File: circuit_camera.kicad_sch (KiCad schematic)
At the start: 25 parts, among them U10 LDO_5-1.8V-(MIC5504-1.8YM5-TR), U8 LM2576HVS-5, U9 LDO 5-3.3V-(MIC5504-3.3YM5-TR)

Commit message: Début PCB
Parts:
- added S1: Switch-SPDT-(EG1218), GAUL-Empreintes:switch-(SW_EG1218), symbol GAUL-Symboles:Switch-SPDT-(EG1218)
- C1LDO1, C1LDO2, C2LDO1, C2LDO2: footprint GAUL-Empreintes:cap-1uF-(CAPC0603X35N) -> Capacitor_SMD:C_0603_1608Metric_Pad1.08x0.95mm_HandSolder
- D1, D4: footprint (none) -> Diode_SMD:D_0603_1608Metric_Pad1.05x0.95mm_HandSolder
- F1, F2: value PTC_resettable_fuse_(MF-MSMF030-2) -> xxmA; footprint MF-MSMF030-2:FUSER_MF-MSMF030-2 -> Fuse:Fuse_0603_1608Metric_Pad1.05x0.95mm_HandSolder
- FB1: footprint (none) -> Inductor_SMD:L_0603_1608Metric_Pad1.05x0.95mm_HandSolder
- Lout1: footprint LM2576:IND_YUDEN_NS12575_YDN -> GAUL-Empreintes:induct-100uH-(IND_YUDEN_NS12575_YDN)
- R30, R31, R32: footprint GAUL-Empreintes:Resistance_TH_classique -> Resistor_SMD:R_0603_1608Metric
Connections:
- net +3.3V: now also S1.2; no longer C2LDO1.1, Cout1.1, Lout1.2, U8.4 (FB), U9.5 (VOUT)
- net GND: now also bornier1.1; no longer bornier1.0 (GND)
- net at F1.1: now also bornier1.2; no longer bornier1.1 (Vbatterie)
- new net: Cout1.1, Lout1.2, S1.1, U8.4 (FB)
- new net: C2LDO1.1, S1.3, U9.5 (VOUT)

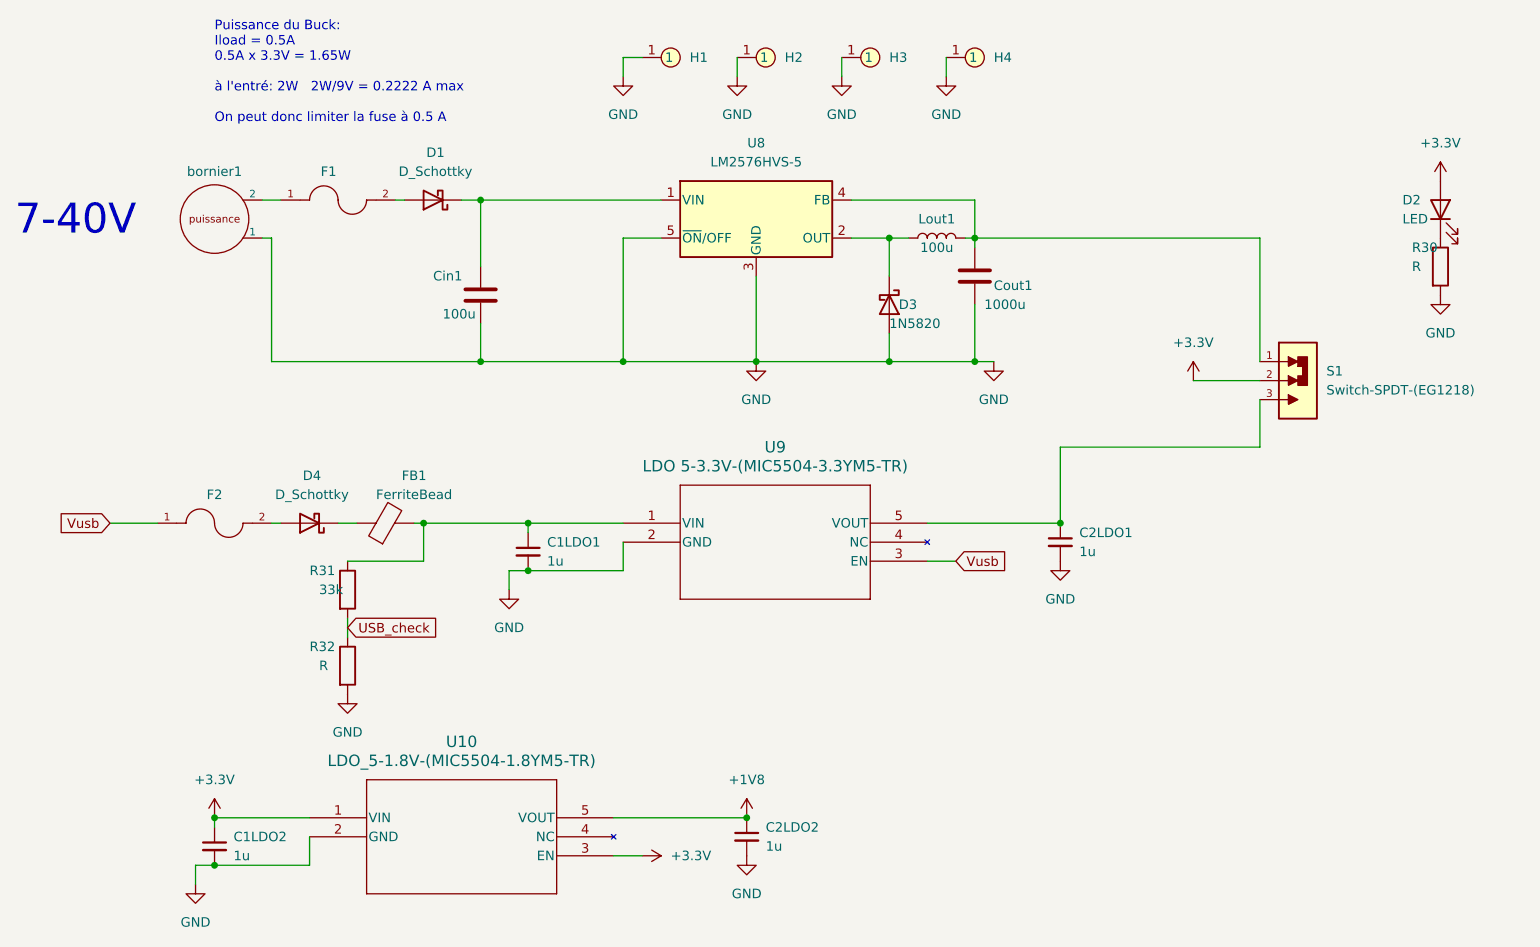
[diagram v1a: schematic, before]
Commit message: Remplacement du Buck par un LDO
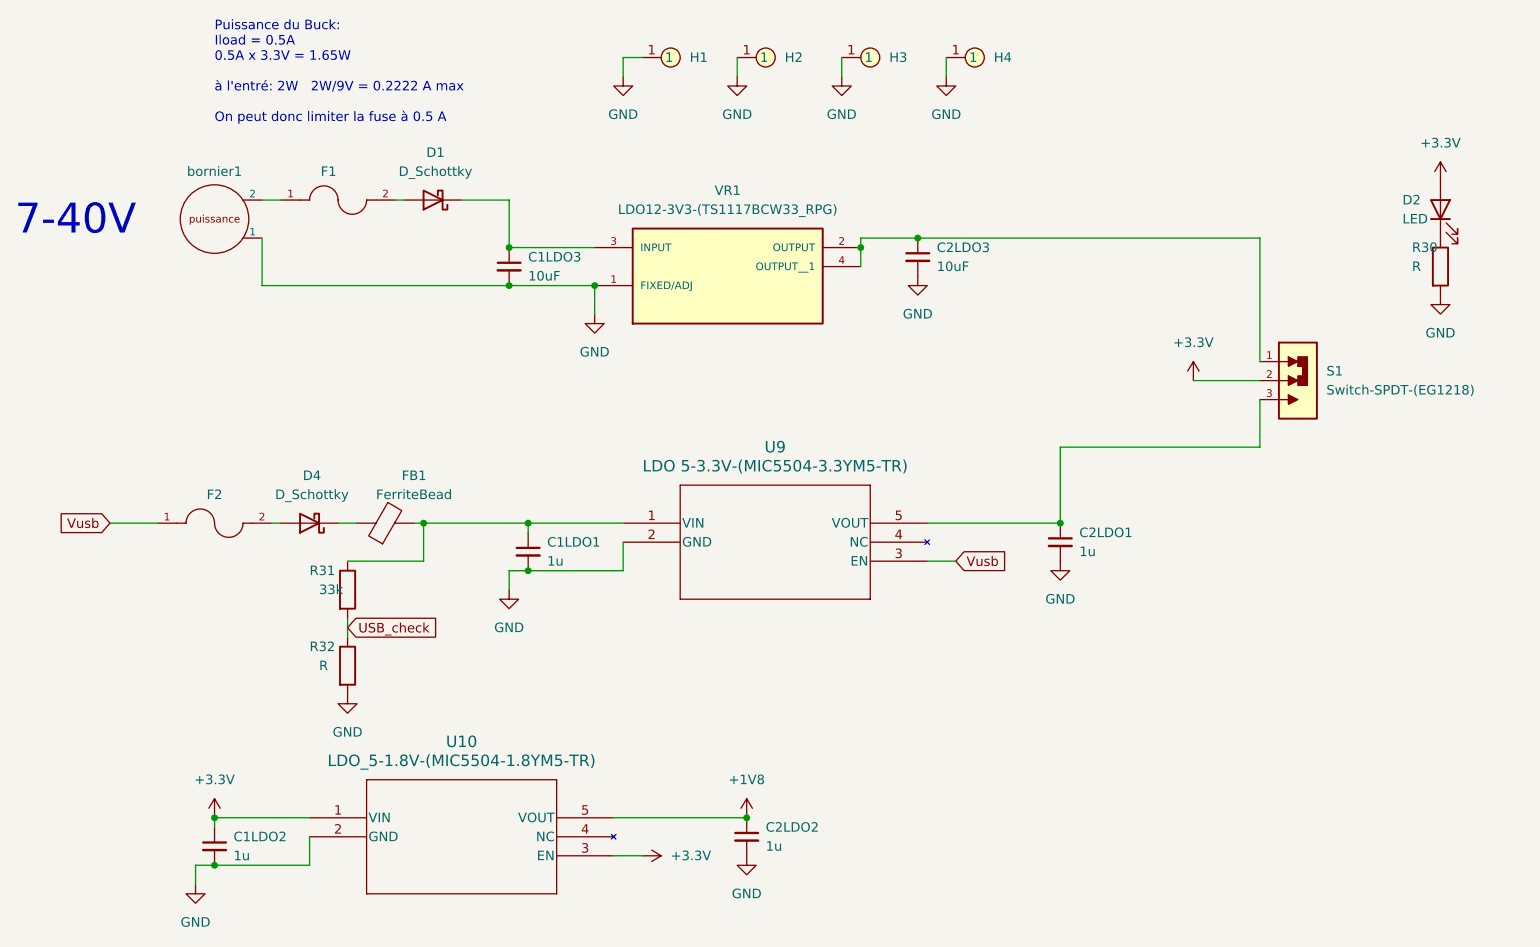
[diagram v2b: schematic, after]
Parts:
- removed Cin1: 100u, Capacitor_THT:CP_Radial_D8.0mm_P3.50mm, symbol Device:C
- removed Cout1: 1000u, Capacitor_THT:CP_Radial_D10.0mm_P5.00mm, symbol Device:C
- removed D3: 1N5820, Diode_THT:D_DO-201AD_P15.24mm_Horizontal, symbol Diode:1N5820
- removed Lout1: 100u, GAUL-Empreintes:induct-100uH-(IND_YUDEN_NS12575_YDN), symbol Device:L
- removed U8: LM2576HVS-5, Package_TO_SOT_SMD:TO-263-5_TabPin3, symbol Regulator_Switching:LM2576HVS-5
- added C1LDO3, C2LDO3: 10uF, Capacitor_SMD:C_0603_1608Metric_Pad1.08x0.95mm_HandSolder, symbol Device:C_Small
- added VR1: LDO12-3V3-(TS1117BCW33_RPG), GAUL-Empreintes:LDO12-3V3-(TS1117BCW33_RPG), symbol GAUL-Symboles:LDO12-3V3-(TS1117BCW33_RPG)
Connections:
- net GND: now also C1LDO3.2, C2LDO3.2, VR1.1 (FIXED/ADJ)
- net at S1.1: now also C2LDO3.1, VR1.2 (OUTPUT), VR1.4 (OUTPUT__1)
- net at D1.1 (K): now also C1LDO3.1, VR1.3 (INPUT)

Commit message: Routing terminé
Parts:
- added H5, H6, H7, H8: ~, GAUL-Empreintes:Ground_mounting_hole_1mm, symbol GAUL-Symboles:Ground_mounting_hole_1mm
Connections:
- net GND: now also H5.1, H6.1, H7.1, H8.1
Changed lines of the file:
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@@
+    (stroke (width 0) (type default))
+  )
+  (wire (pts (xy 196.85 69.85) (xy 196.85 67.31))
     (stroke (width 0) (type default))
   )
@@
     (stroke (width 0) (type default))
   )
+  (wire (pts (xy 227.33 69.85) (xy 227.33 67.31))
+    (stroke (width 0) (type default))
+  )
   (wire (pts (xy 111.76 97.79) (xy 123.19 97.79))
     (stroke (width 0) (type default))
@@
     (stroke (width 0) (type default))
   )
+  (wire (pts (xy 212.09 69.85) (xy 212.09 67.31))
+    (stroke (width 0) (type default))
+  )
   (wire (pts (xy 69.85 175.26) (xy 72.39 175.26))
     (stroke (width 0) (type default))
@@
   )
   (wire (pts (xy 114.3 129.54) (xy 127 129.54))
+    (stroke (width 0) (type default))
+  )
+  (wire (pts (xy 182.88 69.85) (xy 182.88 67.31))
     (stroke (width 0) (type default))
   )
@@
     )
   )
+  (symbol (lib_id "GAUL-Symboles:Ground_mounting_hole_1mm") (at 215.9 64.77 180) (unit 1)
+    (in_bom yes) (on_board yes) (dnp no) (fields_autoplaced)
+    (property "Reference" "H7" (at 218.44 67.31 0)
+      (effects (font (size 1.27 1.27)) (justify right))
+    )
+    (property "Value" "~" (at 215.9 64.77 0)
+      (effects (font (size 1.27 1.27)))
+    )
+    (property "Footprint" "GAUL-Empreintes:Ground_mounting_hole_1mm" (at 215.9 64.77 0)
+      (effects (font (size 1.27 1.27)) hide)
+    )
+    (property "Datasheet" "" (at 215.9 64.77 0)
+      (effects (font (size 1.27 1.27)) hide)
+    )
+    (pin "1")
+    (instances
+      (project "Payload"
+        (path "/5f62c44b-34ee-4720-b187-b4a520863a8a/b731aecd-8fa5-4432-90a5-bb6d0ae39f62"
+          (reference "H7") (unit 1)
+        )
+      )
+      (project "Buck_5V"
+        (path "/b57e233b-724e-41fe-b467-3bde33ee5ca1"
+          (reference "H?") (unit 1)
+        )
+      )
+    )
+  )
   (symbol (lib_id "GAUL-Symboles:Ground_mounting_hole_1mm") (at 133.35 64.77 180) (unit 1)
     (in_bom yes) (on_board yes) (dnp no) (fields_autoplaced)
@@
     )
   )
+  (symbol (lib_id "GAUL-Symboles:Ground_mounting_hole_1mm") (at 186.69 64.77 180) (unit 1)
+    (in_bom yes) (on_board yes) (dnp no) (fields_autoplaced)
+    (property "Reference" "H5" (at 189.23 67.31 0)
+      (effects (font (size 1.27 1.27)) (justify right))
+    )
+    (property "Value" "~" (at 186.69 64.77 0)
+      (effects (font (size 1.27 1.27)))
+    )
+    (property "Footprint" "GAUL-Empreintes:Ground_mounting_hole_1mm" (at 186.69 64.77 0)
+      (effects (font (size 1.27 1.27)) hide)
+    )
+    (property "Datasheet" "" (at 186.69 64.77 0)
+      (effects (font (size 1.27 1.27)) hide)
+    )
+    (pin "1")
+    (instances
+      (project "Payload"
+        (path "/5f62c44b-34ee-4720-b187-b4a520863a8a/b731aecd-8fa5-4432-90a5-bb6d0ae39f62"
+          (reference "H5") (unit 1)
+        )
+      )
+      (project "Buck_5V"
+        (path "/b57e233b-724e-41fe-b467-3bde33ee5ca1"
+          (reference "H?") (unit 1)
+        )
+      )
+    )
+  )
   (symbol (lib_id "power:GND") (at 156.21 69.85 0) (unit 1)
     (in_bom yes) (on_board yes) (dnp no) (fields_autoplaced)
@@
     )
   )
+  (symbol (lib_id "power:GND") (at 196.85 69.85 0) (unit 1)
+    (in_bom yes) (on_board yes) (dnp no) (fields_autoplaced)
+    (property "Reference" "#PWR0145" (at 196.85 76.2 0)
+      (effects (font (size 1.27 1.27)) hide)
+    )
+    (property "Value" "GND" (at 196.85 74.93 0)
+      (effects (font (size 1.27 1.27)))
+    )
+    (property "Footprint" "" (at 196.85 69.85 0)
+      (effects (font (size 1.27 1.27)) hide)
+    )
+    (property "Datasheet" "" (at 196.85 69.85 0)
+      (effects (font (size 1.27 1.27)) hide)
+    )
+    (pin "1")
+    (instances
+      (project "Payload"
+        (path "/5f62c44b-34ee-4720-b187-b4a520863a8a/b731aecd-8fa5-4432-90a5-bb6d0ae39f62"
+          (reference "#PWR0145") (unit 1)
+        )
+      )
+      (project "Buck_5V"
+        (path "/b57e233b-724e-41fe-b467-3bde33ee5ca1"
+          (reference "#PWR?") (unit 1)
+        )
+      )
+    )
+  )
   (symbol (lib_id "GAUL-Symboles:Ground_mounting_hole_1mm") (at 160.02 64.77 180) (unit 1)
     (in_bom yes) (on_board yes) (dnp no) (fields_autoplaced)
@@
     )
   )
+  (symbol (lib_id "GAUL-Symboles:Ground_mounting_hole_1mm") (at 231.14 64.77 180) (unit 1)
+    (in_bom yes) (on_board yes) (dnp no) (fields_autoplaced)
+    (property "Reference" "H8" (at 233.68 67.31 0)
+      (effects (font (size 1.27 1.27)) (justify right))
+    )
+    (property "Value" "~" (at 231.14 64.77 0)
+      (effects (font (size 1.27 1.27)))
+    )
+    (property "Footprint" "GAUL-Empreintes:Ground_mounting_hole_1mm" (at 231.14 64.77 0)
+      (effects (font (size 1.27 1.27)) hide)
+    )
+    (property "Datasheet" "" (at 231.14 64.77 0)
+      (effects (font (size 1.27 1.27)) hide)
+    )
+    (pin "1")
+    (instances
+      (project "Payload"
+        (path "/5f62c44b-34ee-4720-b187-b4a520863a8a/b731aecd-8fa5-4432-90a5-bb6d0ae39f62"
+          (reference "H8") (unit 1)
+        )
+      )
+      (project "Buck_5V"
+        (path "/b57e233b-724e-41fe-b467-3bde33ee5ca1"
+          (reference "H?") (unit 1)
+        )
+      )
+    )
+  )
   (symbol (lib_id "Device:C_Small") (at 166.37 93.98 0) (unit 1)
     (in_bom yes) (on_board yes) (dnp no) (fields_autoplaced)
@@
     )
   )
+  (symbol (lib_id "power:GND") (at 182.88 69.85 0) (unit 1)
+    (in_bom yes) (on_board yes) (dnp no) (fields_autoplaced)
+    (property "Reference" "#PWR0144" (at 182.88 76.2 0)
+      (effects (font (size 1.27 1.27)) hide)
+    )
+    (property "Value" "GND" (at 182.88 74.93 0)
+      (effects (font (size 1.27 1.27)))
+    )
+    (property "Footprint" "" (at 182.88 69.85 0)
+      (effects (font (size 1.27 1.27)) hide)
+    )
+    (property "Datasheet" "" (at 182.88 69.85 0)
+      (effects (font (size 1.27 1.27)) hide)
+    )
+    (pin "1")
+    (instances
+      (project "Payload"
+        (path "/5f62c44b-34ee-4720-b187-b4a520863a8a/b731aecd-8fa5-4432-90a5-bb6d0ae39f62"
+          (reference "#PWR0144") (unit 1)
+        )
+      )
+      (project "Buck_5V"
+        (path "/b57e233b-724e-41fe-b467-3bde33ee5ca1"
+          (reference "#PWR?") (unit 1)
+        )
+      )
+    )
+  )
   (symbol (lib_id "power:GND") (at 123.19 101.6 0) (unit 1)
     (in_bom yes) (on_board yes) (dnp no) (fields_autoplaced)
@@
         (path "/5f62c44b-34ee-4720-b187-b4a520863a8a/b731aecd-8fa5-4432-90a5-bb6d0ae39f62"
           (reference "D4") (unit 1)
+        )
+      )
+    )
+  )
+  (symbol (lib_id "GAUL-Symboles:Ground_mounting_hole_1mm") (at 200.66 64.77 180) (unit 1)
+    (in_bom yes) (on_board yes) (dnp no) (fields_autoplaced)
+    (property "Reference" "H6" (at 203.2 67.31 0)
+      (effects (font (size 1.27 1.27)) (justify right))
+    )
+    (property "Value" "~" (at 200.66 64.77 0)
+      (effects (font (size 1.27 1.27)))
+    )
+    (property "Footprint" "GAUL-Empreintes:Ground_mounting_hole_1mm" (at 200.66 64.77 0)
+      (effects (font (size 1.27 1.27)) hide)
+    )
+    (property "Datasheet" "" (at 200.66 64.77 0)
+      (effects (font (size 1.27 1.27)) hide)
+    )
+    (pin "1")
+    (instances
+      (project "Payload"
+        (path "/5f62c44b-34ee-4720-b187-b4a520863a8a/b731aecd-8fa5-4432-90a5-bb6d0ae39f62"
+          (reference "H6") (unit 1)
+        )
+      )
+      (project "Buck_5V"
+        (path "/b57e233b-724e-41fe-b467-3bde33ee5ca1"
+          (reference "H?") (unit 1)
         )
       )
@@
         )
       )
+    )
+  )
+  (symbol (lib_id "power:GND") (at 212.09 69.85 0) (unit 1)
+    (in_bom yes) (on_board yes) (dnp no) (fields_autoplaced)
+    (property "Reference" "#PWR0146" (at 212.09 76.2 0)
+      (effects (font (size 1.27 1.27)) hide)
+    )
+    (property "Value" "GND" (at 212.09 74.93 0)
+      (effects (font (size 1.27 1.27)))
+    )
+    (property "Footprint" "" (at 212.09 69.85 0)
+      (effects (font (size 1.27 1.27)) hide)
+    )
+    (property "Datasheet" "" (at 212.09 69.85 0)
+      (effects (font (size 1.27 1.27)) hide)
+    )
+    (pin "1")
+    (instances
+      (project "Payload"
+        (path "/5f62c44b-34ee-4720-b187-b4a520863a8a/b731aecd-8fa5-4432-90a5-bb6d0ae39f62"
+          (reference "#PWR0146") (unit 1)
+        )
+      )
+      (project "Buck_5V"
+        (path "/b57e233b-724e-41fe-b467-3bde33ee5ca1"
+          (reference "#PWR?") (unit 1)
+        )
+      )
+    )
+  )
+  (symbol (lib_id "power:GND") (at 227.33 69.85 0) (unit 1)
+    (in_bom yes) (on_board yes) (dnp no) (fields_autoplaced)
+    (property "Reference" "#PWR0147" (at 227.33 76.2 0)
+      (effects (font (size 1.27 1.27)) hide)
+    )
+    (property "Value" "GND" (at 227.33 74.93 0)
+      (effects (font (size 1.27 1.27)))
+    )
+    (property "Footprint" "" (at 227.33 69.85 0)
+      (effects (font (size 1.27 1.27)) hide)
+    )
+    (property "Datasheet" "" (at 227.33 69.85 0)
+      (effects (font (size 1.27 1.27)) hide)
+    )
+    (pin "1")
+    (instances
+      (project "Payload"
+        (path "/5f62c44b-34ee-4720-b187-b4a520863a8a/b731aecd-8fa5-4432-90a5-bb6d0ae39f62"
+          (reference "#PWR0147") (unit 1)
+        )
+      )
+      (project "Buck_5V"
+        (path "/b57e233b-724e-41fe-b467-3bde33ee5ca1"
+          (reference "#PWR?") (unit 1)
+        )
+      )
